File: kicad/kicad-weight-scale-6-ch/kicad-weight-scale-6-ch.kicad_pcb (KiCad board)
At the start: 2 copper layers, 100 x 100 mm, 44 parts, among them J1 Barrel_Jack_Switch, J2 Conn_01x02, J3 Conn_01x04, J4 Conn_01x04, J5 Conn_01x04, J6 Conn_01x02, J7 Conn_01x02, J8 Conn_01x02, J9 Conn_01x02, Q1 Si4542DY, Q2 Si4542DY, Q3 BSS138, SW1 SW_Push, U1 TP-4056, U10 USB_Type_C, U11 USB_Type_C, U12 USB_Type_C, U13 USB_Type_C, U2 StepUpTo5V, U3 WCMCU-ADS1232, U4 ESPWROOM32, U5 WCMCU-ADS1232, U6 DataLoggingBoard, U7 WCMCU-ADS1232, U8 USB_Type_C, U9 USB_Type_C

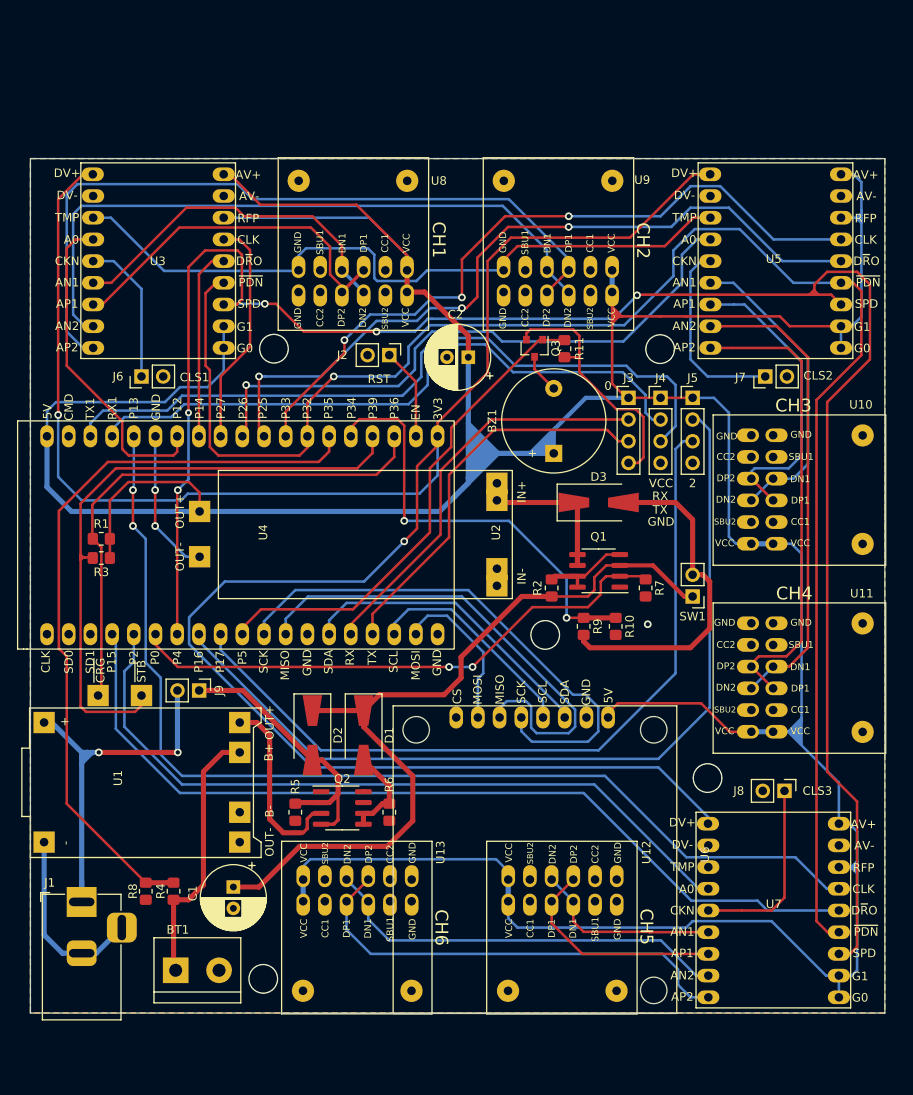
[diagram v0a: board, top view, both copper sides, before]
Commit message: , String to char*, Receive server setup from display
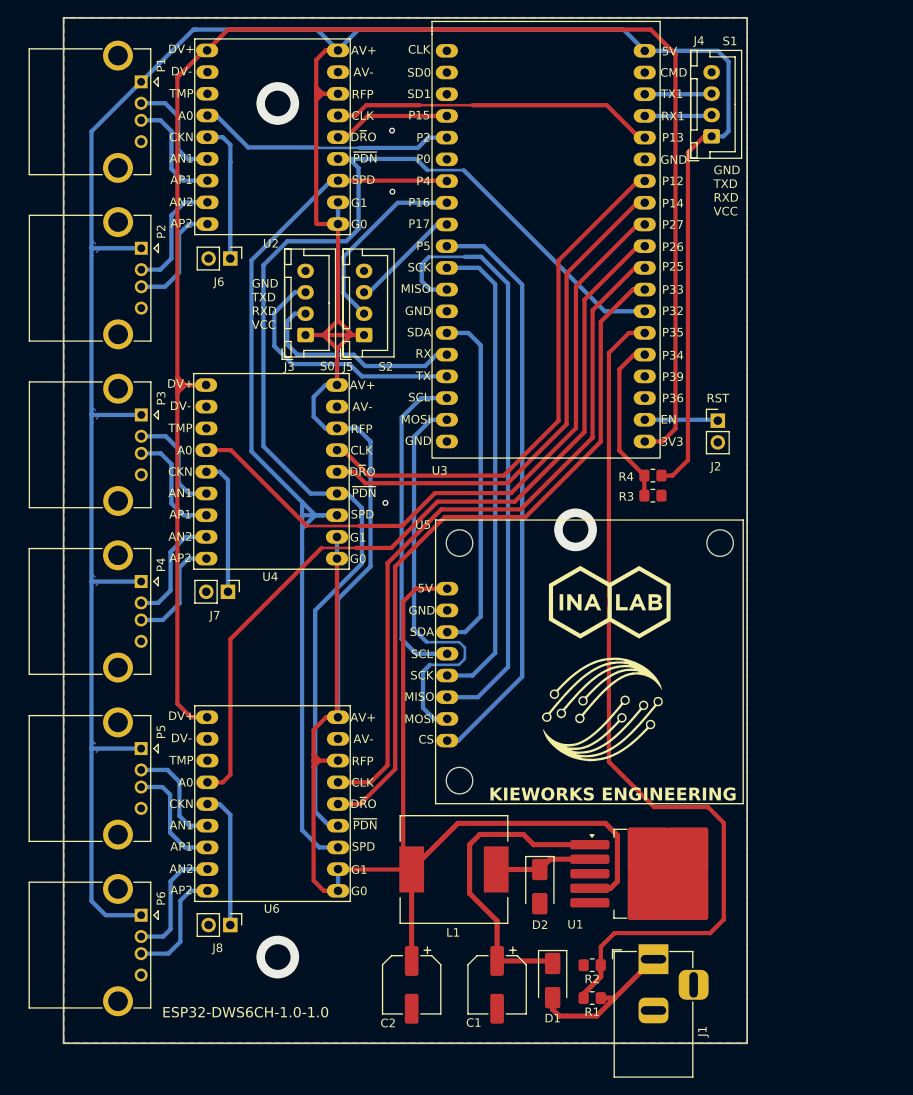
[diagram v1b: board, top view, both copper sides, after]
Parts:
- removed BT1: 18650 Li-ion, TerminalBlock:TerminalBlock_bornier-2_P5.08mm
- removed BZ1: Buzzer, Buzzer_Beeper:Buzzer_12x9.5RM7.6
- removed D3: D_Schottky, Diode_SMD:D_SMA-SMB_Universal_Handsoldering
- removed J9: Conn_01x02, Connector_PinHeader_2.54mm:PinHeader_1x02_P2.54mm_Vertical
- removed Q1, Q2: Si4542DY, Package_SO:SOIC-8_3.9x4.9mm_P1.27mm
- removed Q3: BSS138, Package_TO_SOT_SMD:SOT-23
- removed R10, R11, R5, R6, R7: 1M, Resistor_SMD:R_0805_2012Metric_Pad1.20x1.40mm_HandSolder
- removed R8: 100k, Resistor_SMD:R_0805_2012Metric_Pad1.20x1.40mm_HandSolder
- removed R9: 1k, Resistor_SMD:R_0805_2012Metric_Pad1.20x1.40mm_HandSolder
- removed SW1: SW_Push, Connector_PinHeader_2.54mm:PinHeader_1x02_P2.54mm_Vertical
- removed U10, U11, U12, U13, U8, U9: USB_Type_C, DIY-Board:Type C Converter
- removed U7: WCMCU-ADS1232, DIY-Board:wcmcu-ads1232
- added G***: LOGO, myLogo:keyworks_logo_15, F.Cu at (166.8, 114.5)
- added G***: LOGO, myLogo:inalab_logo_15, F.Cu at (167.8, 101.9)
- added L1: 3.3uH, Inductor_SMD:L_12x12mm_H4.5mm, F.Cu at (149.6, 133.2)
- added P1: CH1, Connector_USB:USB_A_CONNFLY_DS1095-WNR0, F.Cu at (113.0, 41.0)
- added P2: CH1, Connector_USB:USB_A_CONNFLY_DS1095-WNR0, F.Cu at (113.0, 60.5)
- added P3: CH1, Connector_USB:USB_A_CONNFLY_DS1095-WNR0, F.Cu at (113.0, 80.0)
- added P4: CH1, Connector_USB:USB_A_CONNFLY_DS1095-WNR0, F.Cu at (113.0, 99.5)
- added P5: CH1, Connector_USB:USB_A_CONNFLY_DS1095-WNR0, F.Cu at (113.0, 119.0)
- added P6: CH1, Connector_USB:USB_A_CONNFLY_DS1095-WNR0, F.Cu at (113.0, 138.6)
- C1: value 220u -> 680uF; footprint Capacitor_THT:CP_Radial_D7.5mm_P2.50mm -> Capacitor_SMD:CP_Elec_6.3x9.9
- C2: value 100U -> 220uF; footprint Capacitor_THT:CP_Radial_D7.5mm_P2.50mm -> Capacitor_SMD:CP_Elec_6.3x9.9
- D1, D2: value D_Schottky -> 1N5824; footprint Diode_SMD:D_SMA-SMB_Universal_Handsoldering -> Diode_SMD:D_SMA
- J1: value Barrel_Jack_Switch -> 9VDC
- J2: value Conn_01x02 -> Reset
- J3: value Conn_01x04 -> Serial; footprint Connector_PinHeader_2.54mm:PinHeader_1x04_P2.54mm_Vertical -> Connector_JST:JST_XH_B4B-XH-A_1x04_P2.50mm_Vertical
- J4: value Conn_01x04 -> Serial1; footprint Connector_PinHeader_2.54mm:PinHeader_1x04_P2.54mm_Vertical -> Connector_JST:JST_XH_B4B-XH-A_1x04_P2.50mm_Vertical
- J5: value Conn_01x04 -> Serial2; footprint Connector_PinHeader_2.54mm:PinHeader_1x04_P2.54mm_Vertical -> Connector_JST:JST_XH_B4B-XH-A_1x04_P2.50mm_Vertical
- R1: value 10k -> 27k
- R2: value 10k -> 100k
- R3: value 10k -> 47k
- R4: value 27k -> 47k
- U1: value TP-4056 -> LM2596S-5; footprint DIY-Board:Li-ion ic charger -> Package_TO_SOT_SMD:TO-263-5_TabPin3
- U2: value StepUpTo5V -> WCMCU-ADS1232; footprint DIY-Board:Step up 5V -> DIY-Board:wcmcu-ads1232
- U3: value WCMCU-ADS1232 -> ESPWROOM32; footprint DIY-Board:wcmcu-ads1232 -> DIY-Board:esp wroom 32 board
- U4: value ESPWROOM32 -> WCMCU-ADS1232; footprint DIY-Board:esp wroom 32 board -> DIY-Board:wcmcu-ads1232
- U5: value WCMCU-ADS1232 -> DataLoggingBoard; footprint DIY-Board:wcmcu-ads1232 -> DIY-Board:Datalogging board
- U6: value DataLoggingBoard -> WCMCU-ADS1232; footprint DIY-Board:Datalogging board -> DIY-Board:wcmcu-ads1232
- moved R1 78.7 mm to (165.8, 148.2)
- moved C2 73.7 mm to (144.6, 146.7), turned to -90 degrees
- moved R4 72.7 mm to (172.8, 89.5), turned to 0 degrees
- moved J7 67.7 mm to (123.1, 100.7), turned to -90 degrees
- moved J1 67.3 mm to (172.9, 143.7)
- moved J8 66.7 mm to (123.4, 139.7)
- moved R3 65.3 mm to (172.8, 87.1)
- moved U1 61.1 mm to (173.1, 133.7), turned to 0 degrees
- moved U5 52.1 mm to (165.1, 109.2), turned to 0 degrees
- moved U2 47.5 mm to (128.4, 47.5), turned to 180 degrees
- moved U3 45.4 mm to (160.4, 60.5)
- moved R2 44.4 mm to (165.8, 144.4), turned to 180 degrees
- moved J2 39.2 mm to (180.4, 80.7), turned to 0 degrees
- moved J5 39.1 mm to (139.1, 70.7), turned to 90 degrees
- moved J3 38.5 mm to (132.2, 70.7), turned to 90 degrees
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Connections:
- C1 pad 1: VCC_1 -> Net-(D1-K)
- D1 pad 1: VCC_1 -> Net-(D1-K)
- D1 pad 2: Net-(D1-Pad2) -> VBAT
- D2 pad 1: VCC_1 -> Net-(D2-K)
- D2 pad 2: 5V -> GND
- J1 pad 1: Net-(J1-Pad1) -> VBAT
- R1 pad 1: VCC -> VBAT
- R1 pad 2: ~CHRG -> VBAT_SENSE
- R2 pad 1: VCC_1 -> VBAT_SENSE
- R2 pad 2: Net-(Q1-Pad4) -> GND
- R3 pad 2: ~STDBY -> VCC_SENSE
- R4 pad 1: VCC_B -> VCC_SENSE
- R4 pad 2: VCC_B_SENSE -> GND
- U1 pad 1: VCC_B1 -> Net-(D1-K)
- U1 pad 2: VCC_B -> Net-(D2-K)
- U1 pad 4: GND -> VCC
- U2 pad 1: VCC_2 -> VCC
- U2 pad 2: GND -> VCC
- U2 pad 3: VCC -> SPEED
- U2 pad 4: GND -> ~{PWDN}
- U3 pad 1: VCC -> 3V3
- U3 pad 10: 3V3 -> A0_3
- U3 pad 11: GND -> A0_2
- U3 pad 12: GND -> DATA_2
- U3 pad 13: A0_1 -> SCLK_2
- U3 pad 14: CLKIN_1 -> GND
- U3 pad 15: AINN1_1 -> SCLK_1
- U3 pad 16: AINP1_1 -> RXD1
- U3 pad 17: AINN2_1 -> TXD1
- U3 pad 18: AINP2_1 -> unconnected-(U3-11/CSC/CMD-Pad18)
- U3 pad 2: VCC -> EN
- U3 pad 3: SPEED -> unconnected-(U3-36/ADC0-Pad3)
- U3 pad 4: ~PWDN -> unconnected-(U3-39/ADC3-Pad4)
- U3 pad 5: DATA_1 -> VCC_SENSE
- U3 pad 6: SCLK_1 -> VBAT_SENSE
- U3 pad 7: VCC -> ~{PWDN}
- U3 pad 8: GND -> DATA_3
- U3 pad 9: VCC -> SCLK_3
- U4 pad 1: 3V3 -> VCC
- U4 pad 10: A0_2 -> 3V3
- U4 pad 11: SCLK_1 -> GND
- U4 pad 12: DATA_1 -> GND
- U4 pad 13: A0_1 -> A0_2
- U4 pad 14: GND -> CLKIN_2
- U4 pad 15: SCLK_3 -> AINN1_2
- U4 pad 16: RXD1 -> AINP1_2
- U4 pad 17: TXD1 -> AINN2_2
- U4 pad 18: Net-(U4-Pad18) -> AINP2_2
- U4 pad 2: EN -> VCC
- U4 pad 3: ~CHRG -> SPEED
- U4 pad 4: ~STDBY -> ~{PWDN}
- U4 pad 5: VCC_SENSE -> DATA_2
- U4 pad 6: VCC_B_SENSE -> SCLK_2
- U4 pad 7: ~PWDN -> VCC
- U4 pad 8: SCLK_2 -> GND
- U4 pad 9: DATA_2 -> VCC
- U5 pad 2: VCC -> GND
- U5 pad 3: SPEED -> SDA
- U5 pad 4: ~PWDN -> SCL
- U5 pad 5: DATA_2 -> SCK
- U5 pad 6: SCLK_2 -> MISO
- U5 pad 7: VCC -> MOSI
- U5 pad 8: GND -> CS
- U6 pad 2: GND -> VCC
- U6 pad 3: SDA -> SPEED
- U6 pad 4: SCL -> ~{PWDN}
- U6 pad 5: SCK -> DATA_3
- U6 pad 6: MISO -> SCLK_3
- U6 pad 7: MOSI -> VCC
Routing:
- net ~PWDN: track 197.4 -> 0.00 mm, vias 1 -> 0
- net GND: track 153.1 -> 0.00 mm, vias 8 -> 6
- net ~{PWDN}: track 0.00 -> 143.0 mm
- net SPEED: track 228.6 -> 110.3 mm, vias 5 -> 0
- net VBAT_SENSE: track 0.00 -> 103.3 mm
- net VCC_1: track 94.8 -> 0.00 mm
- net VCC_B_SENSE: track 87.3 -> 0.00 mm
- net RXD2: track 103.8 -> 22.4 mm
- net TXD2: track 92.3 -> 13.0 mm
- net TXD1: track 85.4 -> 7.85 mm
- net AINP2_1: track 87.7 -> 13.4 mm
- net ~STDBY: track 73.7 -> 0.00 mm
- net CS: track 0.00 -> 68.4 mm
- net RXD1: track 76.0 -> 7.87 mm
- net VCC_CNTRL: track 65.1 -> 0.00 mm, vias 2 -> 0
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- added copper zone on B.Cu, net SPEED
- added copper zone on B.Cu, net VCC
- added copper zone on F.Cu, net VCC
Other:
- board size 100 x 100 mm -> 80 x 120 mm
- net class Default removed
- board text added: "AN2"
- board text added: "ESP32-DWS6CH-1.0-1.0"
- board text added: "GND TXD RXD VCC"
- board text added: "KIEWORKS ENGINEERING"
- board text added: "S0"
- board text added: "S1"
- board text added: "S2"
- board text removed: "0"
- board text removed: "2"
- board text removed: "CH1"
- board text removed: "CH2"
- board text removed: "CH3"
- board text removed: "CH4"
- board text removed: "CH5"
- board text removed: "CH6"
- board text removed: "CLS1"
- board text removed: "CLS2"
- board text removed: "CLS3"
- board text removed: "GND"
- board text removed: "RX"
- board text removed: "TX"
- board text removed: "VCC"
